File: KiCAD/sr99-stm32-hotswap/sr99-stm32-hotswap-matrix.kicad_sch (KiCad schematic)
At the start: 227 parts, among them SW1 Esc, SW10 F9, SW100 Alt-CapsL, SW101 Alt-Menu, SW102 Alt-Fn2, SW103 74HC1G66, SW104 74HC1G66, SW11 F10, SW12 F11, SW13 F12, SW14 F13, SW15 F14, SW16 F15, SW17 F16, SW18 F17, SW19 Tdl, SW2 F1, SW20 1, SW21 2, SW22 3, SW23 4, SW24 5, SW25 6, SW26 7, SW27 8, SW28 9, SW29 0, SW3 F2, SW30 MIN, SW31 PLS, SW32 BS, SW33 NumL, SW34 Div, SW35 Mul, SW36 Sub, SW37 Tab, SW38 Q, SW39 W, SW4 F3, SW40 E, SW41 R, SW42 T, SW43 Y, SW44 U, SW45 I, SW46 O, SW47 P, SW48 [, SW49 ], SW5 F4, SW50 \, SW51 N7, SW52 N8, SW53 N9, SW54 Add, SW55 CapsL, SW56 A, SW57 S, SW58 D, SW59 F, SW6 F5, SW60 G, SW61 H, SW62 J, SW63 K, SW64 L, SW65 ;, SW66 ", SW67 Ent, SW68 N4, SW69 N5, SW7 F6, SW70 N6, SW71 LShft, SW72 Z, SW73 X, SW74 C, SW75 V, SW76 B, SW77 N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

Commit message: wip-2025-11-19
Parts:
- removed D57: 1N4148WS, symbol ts-kicad-lib:D
- removed SW94-5-6-8-1: SW_DIP_x05, symbol Switch:SW_DIP_x05
- added SW71: SW_DIP_x04, ts-kicad-lib:SW_DIP_SPSTx04, symbol Switch:SW_DIP_x04
- D57: renamed from D58; footprint (none) -> Diode_SMD:D_SOD-323_HandSoldering
- D58: renamed from D59; footprint (none) -> Diode_SMD:D_SOD-323_HandSoldering
- D59: renamed from D60; footprint (none) -> Diode_SMD:D_SOD-323_HandSoldering
- D60: renamed from D61; footprint (none) -> Diode_SMD:D_SOD-323_HandSoldering
- R17: footprint (none) -> Resistor_SMD:R_Array_Convex_4x0603
- renumbered C20 to C21, C21 to C22, C22 to C23, C23 to C24, D101 to D100, D102 to D101, D103 to D102, D104 to D103, D105 to D104, D106 to D105, D62 to D61, D63 to D62, D64 to D63, D65 to D64, D66 to D65, D67 to D66, D68 to D67, D69 to D68, D70 to D69, D71 to D70, D72 to D71, D73 to D72, D74 to D73, D75 to D74, D76 to D75, D77 to D76, D78 to D77, D79 to D78, D80 to D79, D81 to D80, D82 to D81, D83 to D82, D84 to D83, D85 to D84, D86 to D85, D87 to D86, D88 to D87, D89 to D88, D90 to D89, D91 to D90, D92 to D91, D93 to D92, D94 to D93, D95 to D94, D96 to D95, D97 to D96, D98 to D97, D99 to D98, D100 to D99, SW99 to SW100, SW100 to SW101, SW101 to SW102, SW102 to SW103, SW103 to SW104, SW104 to SW105, SW71 to SW72, SW72 to SW73, SW73 to SW74, SW74 to SW75, SW75 to SW76, SW76 to SW77, SW77 to SW78, SW78 to SW79, SW79 to SW80, SW80 to SW81, SW81 to SW82, SW82 to SW83, SW83 to SW84, SW84 to SW85, SW85 to SW86, SW86 to SW87, SW87 to SW88, SW88 to SW89, SW89 to SW90, SW90 to SW91, SW91 to SW92, SW92 to SW93, SW93 to SW94, SW94 to SW95, SW95 to SW96, SW96 to SW97, SW97 to SW98, SW98 to SW99, U6 to U7, U7 to U8
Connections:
- net GND: now also ENC1.C, ENC2.C; no longer ENC1.G, ENC2.G
- net ROW5: now also SW71.1, SW71.2, SW71.3, SW71.4
- net at D59.2 (A): now also SW71.6
- net at D58.2 (A): now also SW71.7
- net at D57.2 (A): now also SW71.8
- net at D60.2 (A): now also SW71.5

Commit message: update-2025-11-20
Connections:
- net +3V3: now also R17.7, R17.8, R20.5, R20.7, R20.8; no longer R17.2, R17.4, R20.2, R20.4, R20.8
- net COL4: now also SW71.5; no longer D57.1 (K)
- net COL5: now also SW71.6; no longer D58.1 (K)
- net COL7: now also SW71.7; no longer D59.1 (K)
- net COL8: now also SW71.8; no longer D60.1 (K)
- net ENC_B: now also R17.2; no longer R17.3
- net ENC_C: now also R20.2; no longer R20.3
- net ROW0: now also SW18.1; no longer SW18.2
- net ROW1: now also SW36.1; no longer SW36.2
- net ROW2: now also SW37.1, SW54.1; no longer SW37.2, SW54.2
- net ROW3: now also SW101.2, SW55.1, SW67.1, SW70.1; no longer SW101.1, SW55.2, SW67.2, SW70.2
- net ROW4: now also SW72.1, SW83.1, SW88.1; no longer SW72.2, SW83.2, SW88.2
- net ROW5: now also D57.2 (A), D58.2 (A), D59.2 (A), D60.2 (A), SW103.2, SW93.1, SW99.1; no longer SW103.1, SW71.1, SW71.2, SW71.3, SW71.4, SW93.2, SW99.2
- net XCLk: now also D61.2 (A), SW101.1, SW55.2; no longer SW101.2
- net XF17: now also SW18.2; no longer SW18.1
- net XFn2: now also D100.2 (A), SW103.1, SW95.1; no longer SW103.2
- net XMn: now also D98.2 (A), SW93.2
- net at D73.2 (A): now also SW67.2; no longer SW67.1
- net at ENC2.E, U8.2: now also R20.4; no longer R20.7
- net at ENC1.E, U7.2: now also R20.3; no longer R20.5
- net at D93.2 (A): now also SW88.2; no longer SW88.1
- net at D104.2 (A): now also SW99.2; no longer SW99.1
- net at D38.2 (A): now also SW36.2; no longer SW36.1
- net at D56.2 (A): now also SW54.2; no longer SW54.1
- net at D88.2 (A): now also SW83.2; no longer SW83.1
- net at D39.2 (A): now also SW37.2; no longer SW37.1
- net at D76.2 (A): now also SW70.2; no longer SW70.1
- net at D77.2 (A): now also SW72.2; no longer SW72.1
- new net: D59.1 (K), SW71.2
- new net: D58.1 (K), SW71.3
- new net: D57.1 (K), SW71.4
- new net: D60.1 (K), SW71.1
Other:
- moved on the sheet: D58, D59, D60, SW101, SW103, SW18, SW36, SW37, SW54, SW55, SW67, SW70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

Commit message: wip-2025-11-23
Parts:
- removed unit 4 of R20
- removed unit 3 of R20
- added unit 4 of R19
- added unit 3 of R19
- renumbered R20 to R19, R19 to R20
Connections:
- net +3V3: now also R17.4, R17.6, R19.5, R19.6; no longer R17.7, R19.7
- net ENC_A: now also R17.3; no longer R17.1
- net ENC_B: now also R17.5; no longer R17.2
- net ENC_C: now also R19.4; no longer C24.2, ENC2.B, R19.1, R19.2
- net ROW0: now also SW14.1; no longer SW14.2
- net ROW2: now also SW50.1; no longer SW50.2
- net XF13: now also SW14.2; no longer SW14.1
- net at ENC2.E, U8.2: now also R19.1
- net at D52.2 (A): now also SW50.2; no longer SW50.1
- net at ENC1.E, U7.2: now also R17.1
- new net ENC_D: C24.2, ENC2.B, R19.3
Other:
- moved on the sheet: R17A, R17B, R17C, R17D, R19A, R19B, SW14, SW50

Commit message: wip
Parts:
- C21, C22, C23, C24: footprint Capacitor_SMD:C_0603_1608Metric_Pad1.08x0.95mm_HandSolder -> Capacitor_SMD:C_0402_1005Metric
- R18, R20: footprint Resistor_SMD:R_0603_1608Metric -> Resistor_SMD:R_0402_1005Metric
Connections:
- net ROW5: now also SW103.1; no longer SW103.2
- net XFn2: now also SW103.2; no longer SW103.1
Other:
- moved on the sheet: SW103
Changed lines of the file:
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@@
 	)
 	(junction
+		(at 231.14 162.56)
+		(diameter 0)
+		(color 0 0 0 0)
+	)
+	(junction
 		(at 50.8 104.14)
 		(diameter 0)
@@
 	)
 	(junction
-		(at 231.14 162.56)
-		(diameter 0)
-		(color 0 0 0 0)
-	)
-	(junction
 		(at 203.2 63.5)
 		(diameter 0)
@@
 	(wire
 		(pts
+			(xy 228.6 162.56) (xy 231.14 162.56)
+		)
+		(stroke
+			(width 0)
+			(type default)
+		)
+	)
+	(wire
+		(pts
 			(xy 109.22 162.56) (xy 116.84 162.56)
 		)
@@
 	(wire
 		(pts
-			(xy 220.98 157.48) (xy 223.52 157.48)
-		)
-		(stroke
-			(width 0)
-			(type default)
-		)
-	)
-	(wire
-		(pts
 			(xy 55.88 165.1) (xy 55.88 162.56)
 		)
@@
 	(wire
 		(pts
+			(xy 220.98 157.48) (xy 223.52 157.48)
+		)
+		(stroke
+			(width 0)
+			(type default)
+		)
+	)
+	(wire
+		(pts
 			(xy 165.1 104.14) (xy 177.8 104.14)
 		)
@@
 	(wire
 		(pts
-			(xy 228.6 162.56) (xy 231.14 162.56)
-		)
-		(stroke
-			(width 0)
-			(type default)
-		)
-	)
-	(wire
-		(pts
 			(xy 53.34 175.26) (xy 55.88 175.26)
 		)
@@
 			)
 		)
-		(property "Footprint" "Capacitor_SMD:C_0603_1608Metric_Pad1.08x0.95mm_HandSolder"
+		(property "Footprint" "Capacitor_SMD:C_0402_1005Metric"
 			(at 109.22 182.88 0)
 			(effects
@@
 			)
 		)
-		(property "Footprint" "Resistor_SMD:R_0603_1608Metric"
+		(property "Footprint" "Resistor_SMD:R_0402_1005Metric"
 			(at 147.32 165.1 0)
 			(effects
@@
 			)
 		)
-		(property "Footprint" "Resistor_SMD:R_0603_1608Metric"
+		(property "Footprint" "Resistor_SMD:R_0402_1005Metric"
 			(at 66.04 165.1 0)
 			(effects
@@
 	(symbol
 		(lib_id "ts-keyboard-lib:Momentary_Switch")
-		(at 226.06 160.02 0)
+		(at 226.06 160.02 180)
 		(unit 1)
 		(exclude_from_sim no)
@@
 		(fields_autoplaced yes)
 		(property "Reference" "SW103"
-			(at 226.067 152.4 0)
+			(at 226.053 152.4 0)
 			(effects
 				(font
@@
 		)
 		(property "Value" "Alt-Fn2"
-			(at 226.067 154.94 0)
+			(at 226.053 154.94 0)
 			(effects
 				(font
@@
 			)
 		)
-		(property "Footprint" "Capacitor_SMD:C_0603_1608Metric_Pad1.08x0.95mm_HandSolder"
+		(property "Footprint" "Capacitor_SMD:C_0402_1005Metric"
 			(at 35.56 182.88 0)
 			(effects
@@
 			)
 		)
-		(property "Footprint" "Capacitor_SMD:C_0603_1608Metric_Pad1.08x0.95mm_HandSolder"
+		(property "Footprint" "Capacitor_SMD:C_0402_1005Metric"
 			(at 116.84 182.88 0)
 			(effects
@@
 			)
 		)
-		(property "Footprint" "Capacitor_SMD:C_0603_1608Metric_Pad1.08x0.95mm_HandSolder"
+		(property "Footprint" "Capacitor_SMD:C_0402_1005Metric"
 			(at 27.94 182.88 0)
 			(effects

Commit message: pre-DRC upload
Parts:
- removed SW102: Alt-Menu, ts-keyboard-lib:SW_MX_MillMax_3Pin, symbol ts-keyboard-lib:Momentary_Switch
- removed SW103: Alt-Fn2, ts-keyboard-lib:SW_MX_MillMax_3Pin, symbol ts-keyboard-lib:Momentary_Switch
- R18, R20: footprint Resistor_SMD:R_0402_1005Metric -> Resistor_SMD:R_0603_1608Metric_Pad0.98x0.95mm_HandSolder
- ST1, ST2, ST3, ST4, ST5, ST6: value ~ -> (none)
- SW101: footprint ts-keyboard-lib:SW_MX_MillMax_3Pin -> ts-keyboard-lib:SW_MX_MillMax
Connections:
- net +3V3: now also R18.2, R20.2; no longer R17.4, R17.6, R17.8, R18.1, R19.5, R19.6, R19.8, R20.1
- net COL4: now also SW71.8; no longer SW71.5
- net COL5: now also SW71.7; no longer SW71.6
- net COL7: now also SW71.6; no longer SW71.7
- net COL8: now also SW71.5; no longer SW71.8
- net ENC_B: now also R17.4; no longer R17.5
- net ENC_C: now also R19.3; no longer R19.4
- net ENC_D: now also R19.4; no longer R19.3
- net ROW2: now also SW54.2; no longer SW54.1
- net ROW3: now also SW101.1, SW55.2; no longer SW101.2, SW55.1
- net ROW5: now also SW99.2; no longer SW99.1
- net XCLk: now also SW101.2, SW55.1; no longer SW101.1, SW55.2
- net at D104.2 (A): now also SW99.1; no longer SW99.2
- net ENC1_3V3: now reaches R17.7
- net ENC1_3V3: now also R17.5, R17.6, R17.8, R18.1, SW104.5 (VCC), U7.5
- net at D56.2 (A): now also SW54.1; no longer SW54.2
- net ENC2_3V3: now reaches R19.7
- net ENC2_3V3: now also R19.5, R19.6, R19.8, R20.1, SW105.5 (VCC), U8.5
- removed net ENC1_EN: R18.2, SW104.5 (VCC), U7.5
- removed net ENC2_EN: R20.2, SW105.5 (VCC), U8.5
- no-connect marks 4 -> 2
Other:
- moved on the sheet: D57, D58, D59, D60, R17B, R17D, R18, R19B, R19C, R19D, R20, ST3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

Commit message: ready to order
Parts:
- SW101: footprint ts-keyboard-lib:SW_MX_MillMax -> ts-keyboard-lib:SW_MX_HotSwap
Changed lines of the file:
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@@
 			)
 		)
-		(property "Footprint" "ts-keyboard-lib:SW_MX_MillMax"
+		(property "Footprint" "ts-keyboard-lib:SW_MX_HotSwap"
 			(at 193.04 160.02 0)
 			(hide yes)

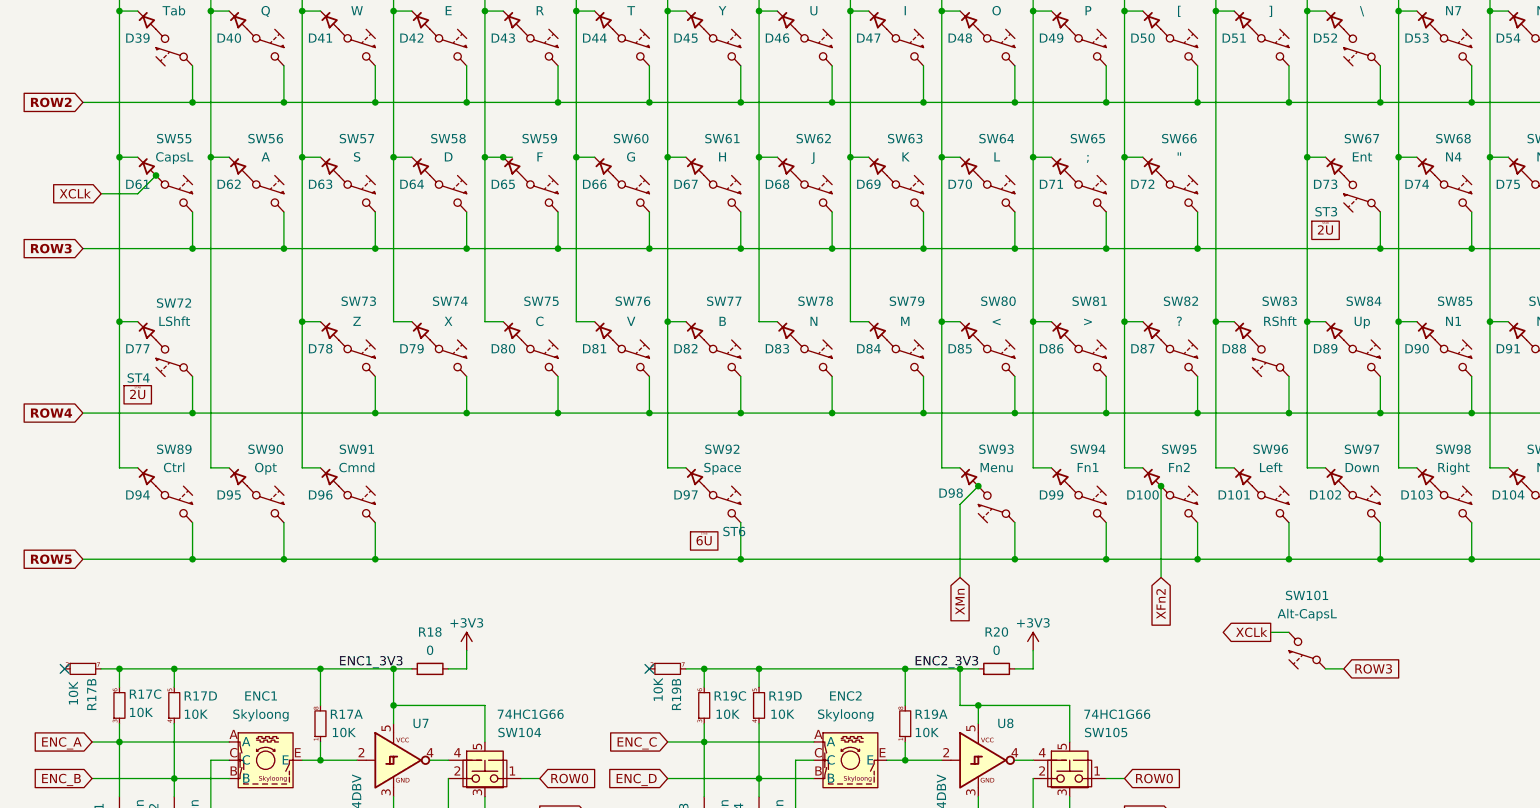
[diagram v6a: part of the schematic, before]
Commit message: removed stepped caps-lock
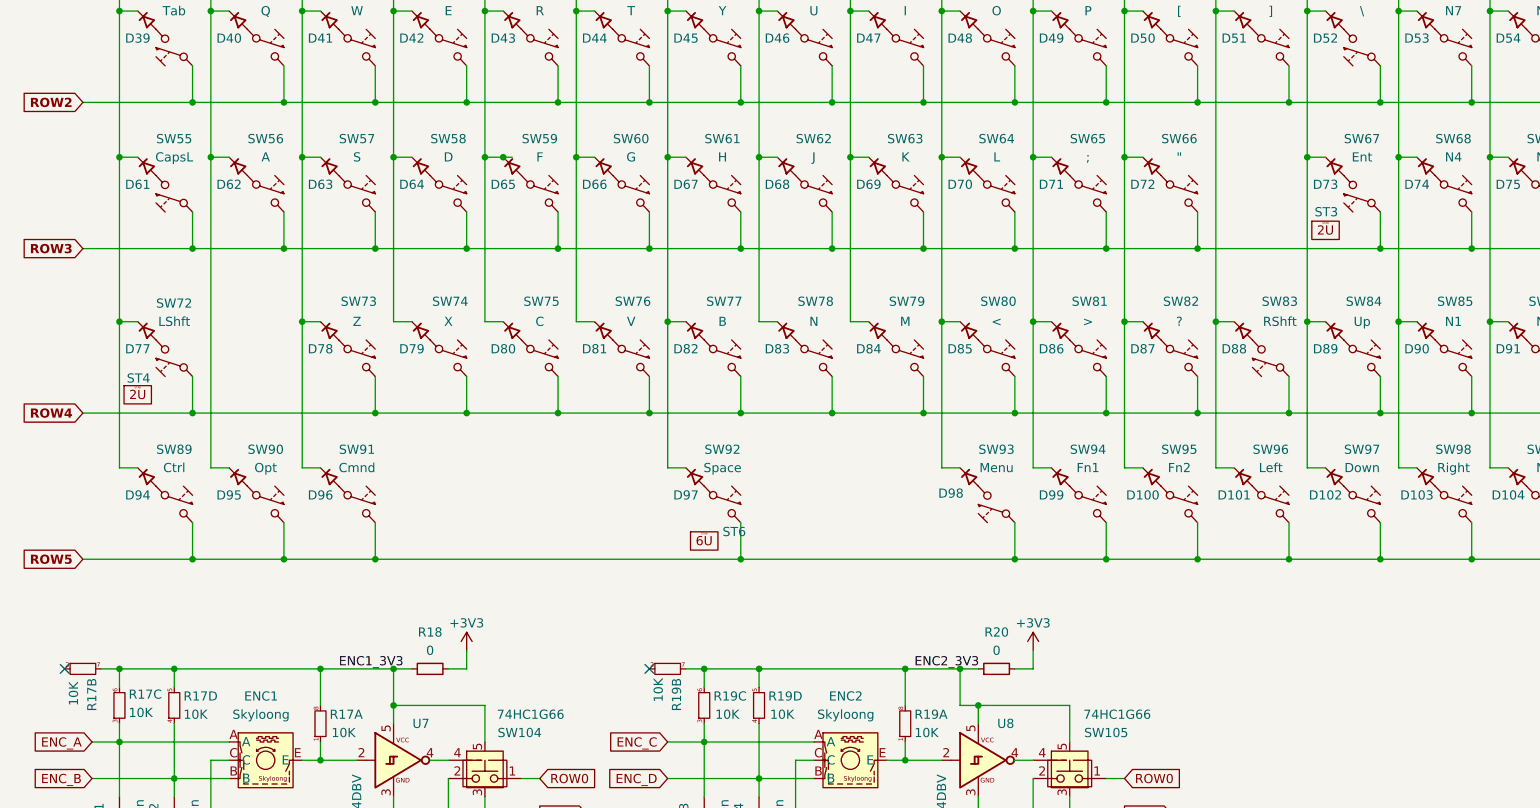
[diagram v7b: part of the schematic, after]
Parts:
- removed SW101: Alt-CapsL, ts-keyboard-lib:SW_MX_HotSwap, symbol ts-keyboard-lib:Momentary_Switch
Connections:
- net ROW3: now also SW55.1; no longer SW55.2
- net XCLk: no longer names the net of D61.2 (A)
- net XCLk: now also SW55.2; no longer SW55.1
- net XFn2: no longer names the net of D100.2 (A), SW95.1
- net XMn: no longer names the net of D98.2 (A), SW93.2
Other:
- moved on the sheet: SW55
